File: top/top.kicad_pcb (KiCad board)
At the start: 4 copper layers, 28.3 x 40 mm, 21 parts, among them P1 CONN_10, P2 CONN_5, P3 CONN_20, U1 IQS572, U4 ESD

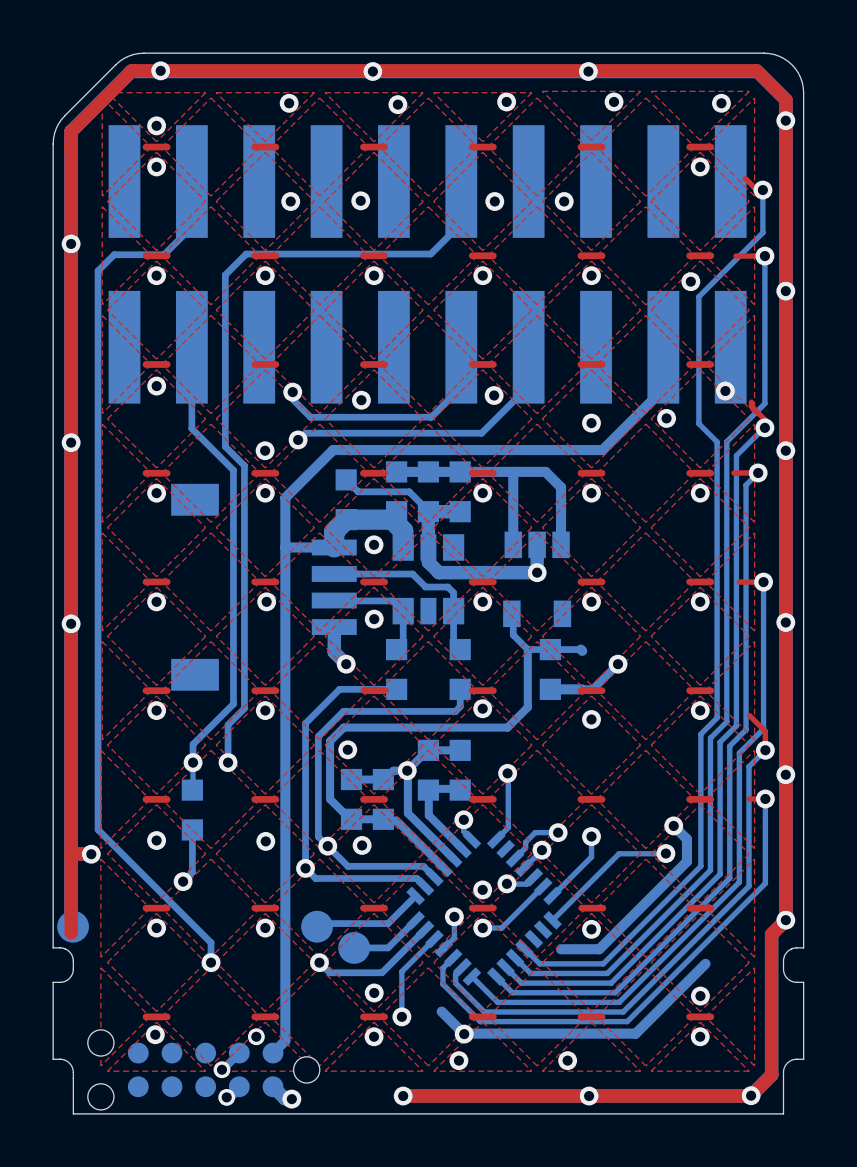
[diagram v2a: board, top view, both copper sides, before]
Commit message: Reposition the FFC connector.
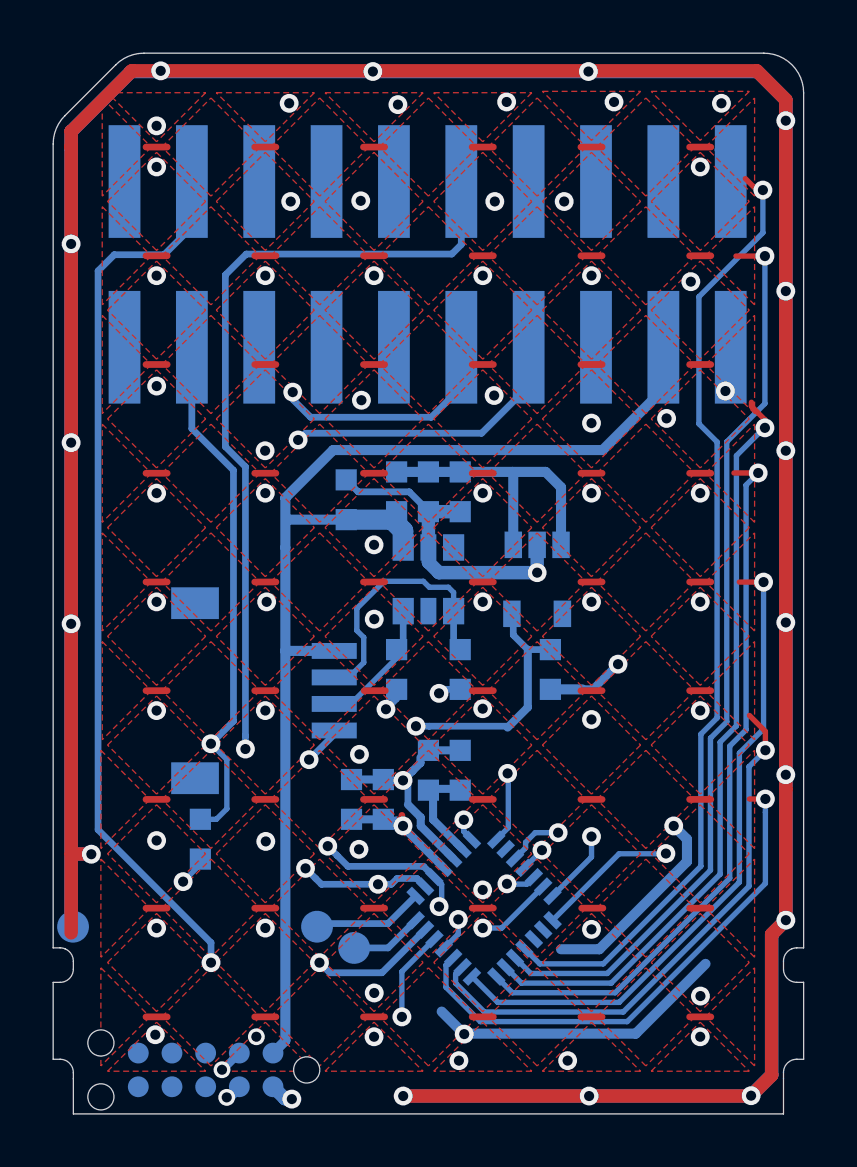
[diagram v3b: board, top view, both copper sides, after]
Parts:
- moved P2 3.90 mm to (196.2, 142.5)
- moved C1 1.14 mm to (197.1, 148.1)
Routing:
- net +3V3: track 20.4 -> 17.4 mm, vias 0 -> 2
- net /SCL_BOTTOM: track 7.04 -> 9.16 mm
- net /RX2: track 46.9 -> 44.8 mm
- net /NRST: track 30.3 -> 31.7 mm
- net /SDA: track 51.8 -> 50.8 mm, vias 3 -> 5
- net /VCC_BOTTOM: track 44.7 -> 45.7 mm
- net /RDY: track 44.6 -> 43.7 mm
- net /SCL: track 55.3 -> 54.4 mm, vias 3 -> 5

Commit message: Replace 47 ohm resistors with 33 ohm ones.
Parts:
- R6, R7: value 47 -> 33
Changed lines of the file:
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@@
   (general
     (thickness 1.6)
-    (drawings 75)
+    (drawings 70)
     (tracks 805)
     (zones 0)
@@
     (at 204 146.6 270)
     (attr smd)
-    (fp_text reference C5 (at 0.6262 2.17 270) (layer B.SilkS)
-      (effects (font (size 0.75 0.75) (thickness 0.15)) (justify mirror))
-    )
-    (fp_text value 1uF (at 0.677 1.1286 270) (layer B.SilkS)
+    (fp_text reference C5 (at 0.6 2.4 270) (layer B.SilkS)
+      (effects (font (size 0.75 0.75) (thickness 0.15)) (justify mirror))
+    )
+    (fp_text value 1uF (at 3.2 2 270) (layer B.SilkS)
       (effects (font (size 0.75 0.75) (thickness 0.15)) (justify mirror))
     )
@@
     (at 210.3 141.7 90)
     (attr smd)
-    (fp_text reference C12 (at -3.0546 3.4664) (layer B.SilkS)
-      (effects (font (size 0.75 0.75) (thickness 0.15)) (justify mirror))
-    )
-    (fp_text value 1uF (at -4.1214 3.4664) (layer B.SilkS)
+    (fp_text reference C12 (at 1 3.5 270) (layer B.SilkS)
+      (effects (font (size 0.75 0.75) (thickness 0.15)) (justify mirror))
+    )
+    (fp_text value 1uF (at -1.5 3.5 90) (layer B.SilkS)
       (effects (font (size 0.75 0.75) (thickness 0.15)) (justify mirror))
     )
@@
     (at 204.5 141.7 90)
     (attr smd)
-    (fp_text reference R7 (at -4.7 -6.4 270) (layer B.SilkS)
-      (effects (font (size 0.75 0.75) (thickness 0.15)) (justify mirror))
-    )
-    (fp_text value 47 (at -6.5 -6.5 90) (layer B.SilkS)
+    (fp_text reference R7 (at 0.7 1.2 90) (layer B.SilkS)
+      (effects (font (size 0.75 0.75) (thickness 0.15)) (justify mirror))
+    )
+    (fp_text value 33 (at -1.1 1.1 90) (layer B.SilkS)
       (effects (font (size 0.75 0.75) (thickness 0.15)) (justify mirror))
     )
@@
     (at 205.7 145.5 270)
     (attr smd)
-    (fp_text reference C4 (at 1.9 0.7 50) (layer B.SilkS)
-      (effects (font (size 0.75 0.75) (thickness 0.15)) (justify mirror))
-    )
-    (fp_text value 100pF (at 4.1 2.6 50) (layer B.SilkS)
+    (fp_text reference C4 (at -1.8 -3.9 270) (layer B.SilkS)
+      (effects (font (size 0.75 0.75) (thickness 0.15)) (justify mirror))
+    )
+    (fp_text value 100pF (at 1 -3.9 270) (layer B.SilkS)
       (effects (font (size 0.75 0.75) (thickness 0.15)) (justify mirror))
     )
@@
     (at 206.9 145.5 270)
     (attr smd)
-    (fp_text reference C3 (at -0.72 -1.1514 90) (layer B.SilkS)
-      (effects (font (size 0.75 0.75) (thickness 0.15)) (justify mirror))
-    )
-    (fp_text value 1uF (at 0.9818 -1.5578) (layer B.SilkS)
+    (fp_text reference C3 (at -1.8 -4.1 90) (layer B.SilkS)
+      (effects (font (size 0.75 0.75) (thickness 0.15)) (justify mirror))
+    )
+    (fp_text value 1uF (at 0.3 -4.1 90) (layer B.SilkS)
       (effects (font (size 0.75 0.75) (thickness 0.15)) (justify mirror))
     )
@@
     (at 206.9 141.7 90)
     (attr smd)
-    (fp_text reference R6 (at -3.7404 -6.621 90) (layer B.SilkS)
-      (effects (font (size 0.75 0.75) (thickness 0.15)) (justify mirror))
-    )
-    (fp_text value 47 (at -5.8486 -6.5448 90) (layer B.SilkS)
+    (fp_text reference R6 (at 0.8 1.3 270) (layer B.SilkS)
+      (effects (font (size 0.75 0.75) (thickness 0.15)) (justify mirror))
+    )
+    (fp_text value 33 (at -1 1.7 90) (layer B.SilkS)
       (effects (font (size 0.75 0.75) (thickness 0.15)) (justify mirror))
     )
@@
     (at 202.8 146.6 270)
     (attr smd)
-    (fp_text reference C6 (at 1.3 1.1742 270) (layer B.SilkS)
-      (effects (font (size 0.75 0.75) (thickness 0.15)) (justify mirror))
-    )
-    (fp_text value 100pF (at 0.0442 2.2664 90) (layer B.SilkS)
+    (fp_text reference C6 (at 0.3 2.4 270) (layer B.SilkS)
+      (effects (font (size 0.75 0.75) (thickness 0.15)) (justify mirror))
+    )
+    (fp_text value 100pF (at 3.1 2.4 90) (layer B.SilkS)
       (effects (font (size 0.75 0.75) (thickness 0.15)) (justify mirror))
     )
@@
   )
   (gr_circle (center 203.9 137.3) (end 204.123607 137.3) (layer B.SilkS) (width 0.15))
-  (gr_line (start 203.5302 143.2052) (end 199.5678 144.4498) (layer B.SilkS) (width 0.254))
-  (gr_line (start 203.5302 143.2306) (end 203.5302 140.5636) (layer B.SilkS) (width 0.254))
-  (gr_line (start 207.2132 143.2306) (end 203.5302 143.2306) (layer B.SilkS) (width 0.254))
-  (gr_line (start 210.312 143.1036) (end 212.3948 144.5768) (layer B.SilkS) (width 0.254))
-  (gr_line (start 208.7118 143.0782) (end 209.4992 144.7292) (layer B.SilkS) (width 0.254))
   (gr_line (start 218.6178 151.7396) (end 218.6178 156.9974) (layer F.Mask) (width 0.6))
   (gr_line (start 219.1766 151.1808) (end 218.6432 151.7142) (layer F.Mask) (width 0.6))
@@
   )
   (gr_line (start 192.2272 121.412) (end 192.2272 151.6634) (layer B.Mask) (width 0.6))
-  (gr_text 84981-4 (at 194.4 138 90) (layer B.SilkS)
+  (gr_text 84981-4 (at 198.9 137.9) (layer B.SilkS)
     (effects (font (size 0.738 0.738) (thickness 0.15)) (justify mirror))
   )

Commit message: Bump top board version to 2.1.0
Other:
- board text added: "PCB_ID: touchpad_top_2.1.0"
- board text removed: "PCB_ID: touchpad_top_2.0.0"
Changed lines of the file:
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@@
   (title_block
     (title "UHK Touchpad Module - Top Board")
-    (rev 2.0.0)
+    (rev 2.1.0)
     (company "Ultimate Gadget Laboratories Kft.")
   )
@@
   (gr_line (start 217.8304 157.7848) (end 218.6178 156.9974) (layer F.Mask) (width 0.6))
   (gr_line (start 204.7 157.7848) (end 217.8 157.7848) (layer F.Mask) (width 0.6))
-  (gr_text "PCB_ID: touchpad_top_2.0.0" (at 205.2 120.3) (layer B.SilkS)
+  (gr_text "PCB_ID: touchpad_top_2.1.0" (at 205.2 120.3) (layer B.SilkS)
     (effects (font (size 0.75 0.75) (thickness 0.15)) (justify mirror))
   )
